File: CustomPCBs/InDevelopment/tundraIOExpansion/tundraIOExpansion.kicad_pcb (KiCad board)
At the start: 2 copper layers, 53 parts, among them J2 Conn_ARM_SWD_TagConnect_TC203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, J3 Conn_ARM_SWD_TagConnect_TC203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, U1 RP2040, U2 MX25L3233FM2, U4 MX25L3233FM2, U5 RP2040, Y1 Crystal, Y2 32.768kHz, Y3 Crystal

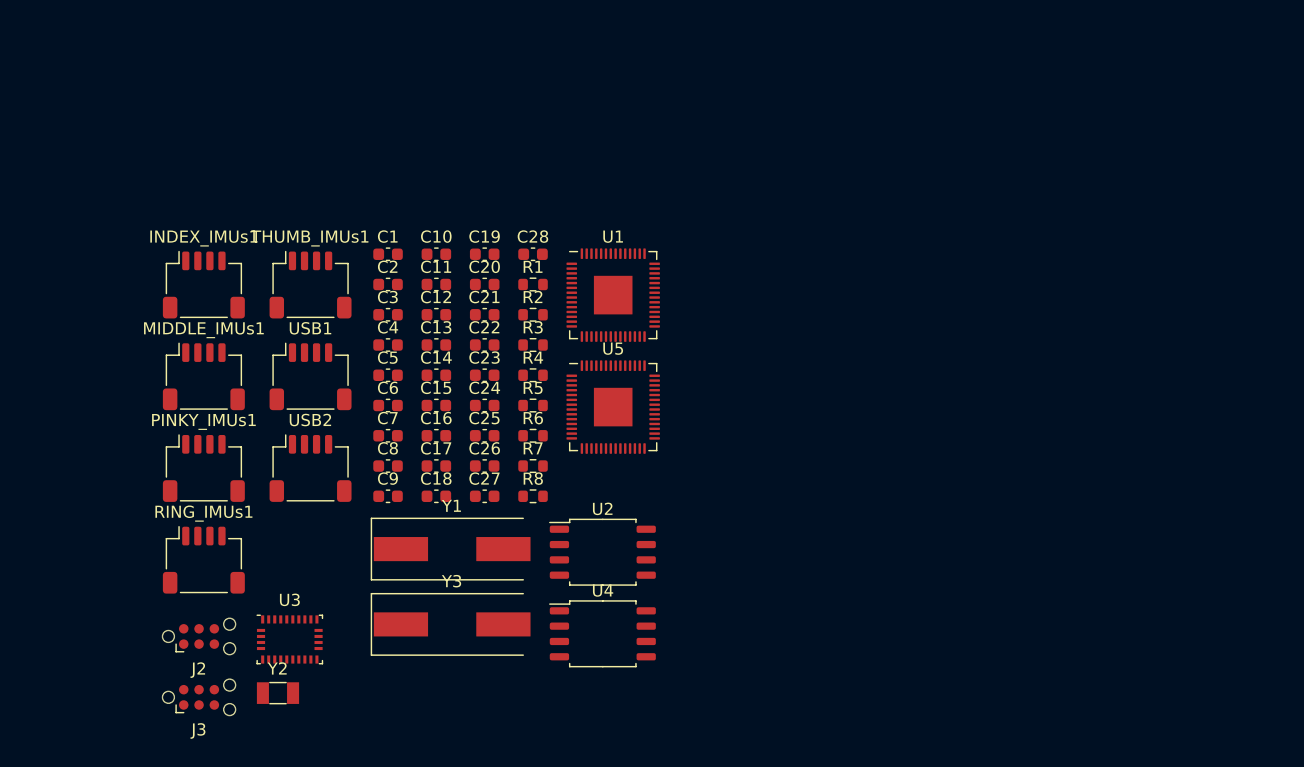
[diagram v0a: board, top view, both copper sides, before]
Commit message: Making outline for PCB
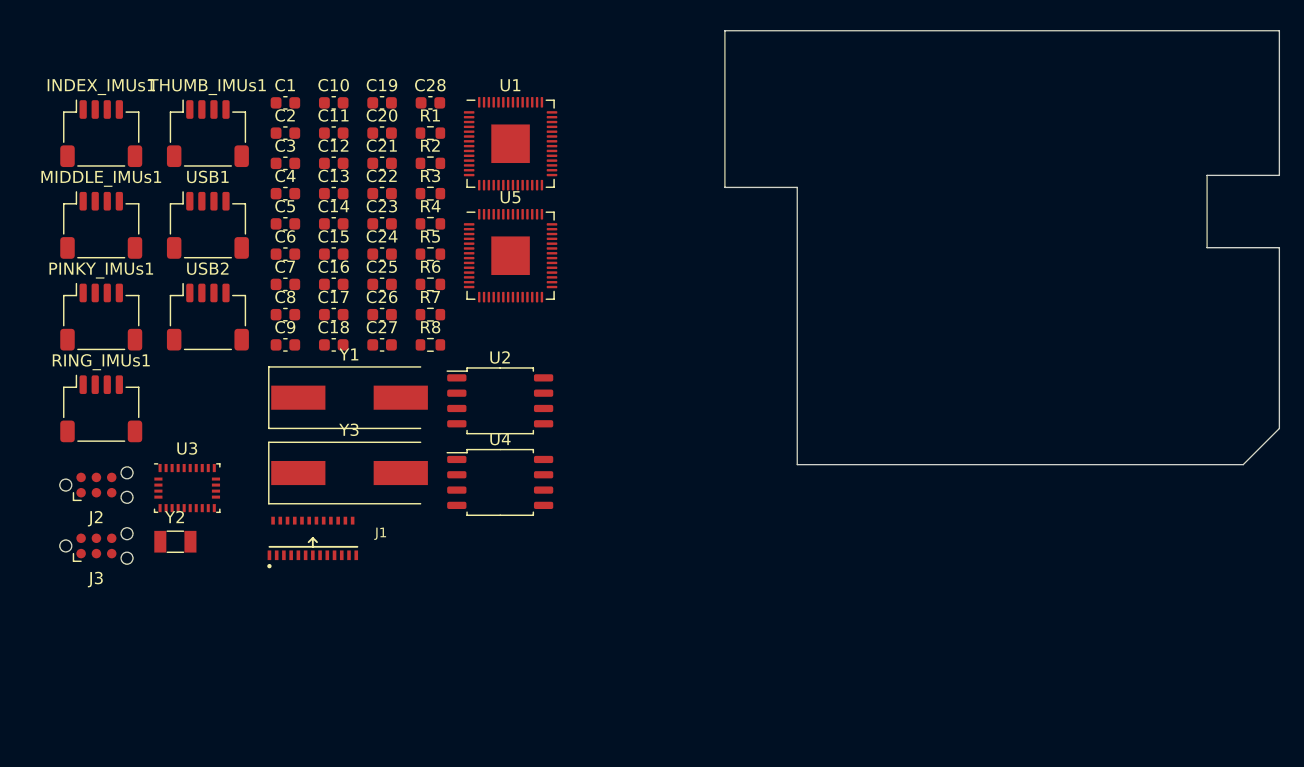
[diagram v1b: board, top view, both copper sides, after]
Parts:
- added J1: Conn_01x25, my_connectors:25PIN FRONT FLIP 0.6mm PITCH AYF332535A, F.Cu at (81.6, 99.2)
- moved THUMB_IMUs1 15.2 mm to (72.9, 65.6)
- moved U1 15.2 mm to (98.0, 66.5)
- moved U2 15.2 mm to (97.1, 87.8)
- moved U3 15.2 mm to (71.2, 95.0)
- moved U4 15.2 mm to (97.1, 94.6)
- moved U5 15.2 mm to (98.0, 75.8)
- moved USB1 15.2 mm to (72.9, 73.2)
- moved USB2 15.2 mm to (72.9, 80.8)
- moved Y1 15.2 mm to (84.6, 87.5)
- moved Y3 15.2 mm to (84.6, 93.8)
- moved J2 15.2 mm to (63.6, 94.8)
- moved J3 15.2 mm to (63.6, 99.8)
- moved C1 15.2 mm to (79.3, 63.1)
- moved C10 15.2 mm to (83.3, 63.1)
- moved C11 15.2 mm to (83.3, 65.6)
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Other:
- board outline added: 46 x 36 mm

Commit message: Connectors and ICs placed on rough locations
Also took care of board layout curves
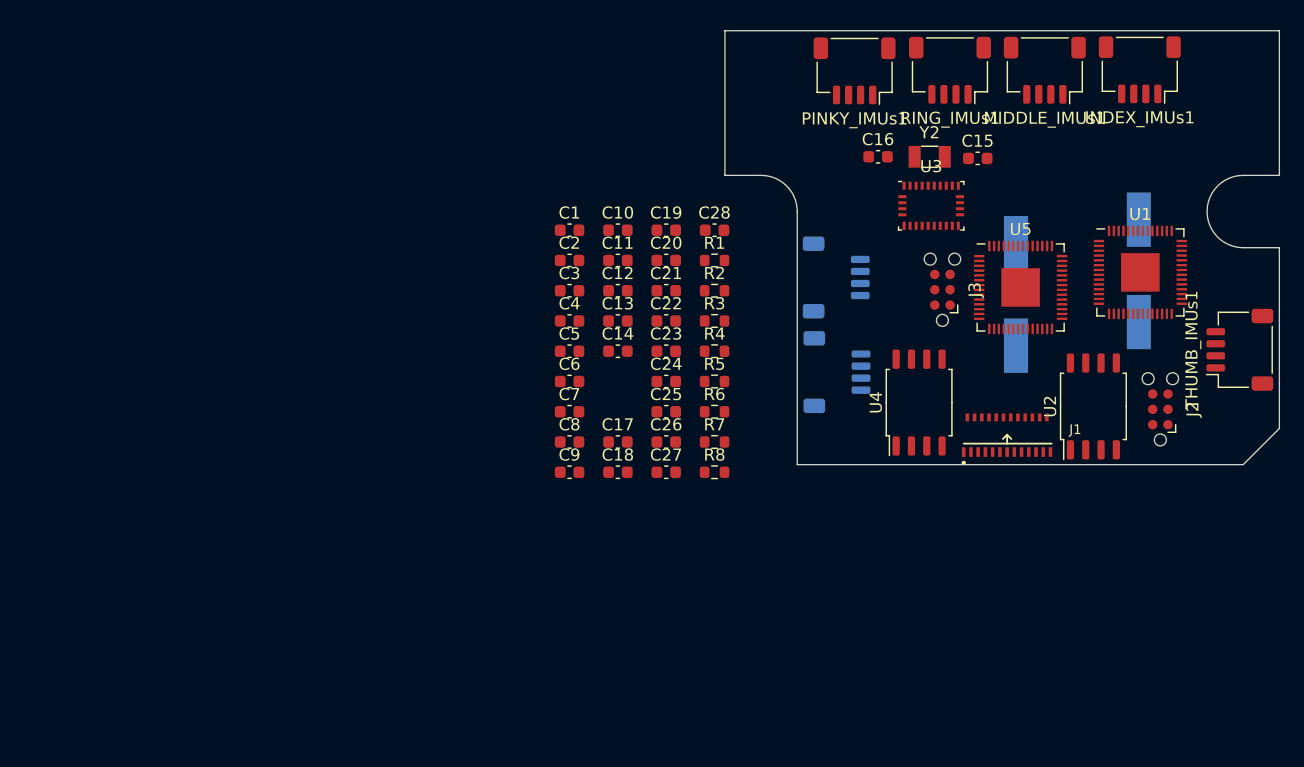
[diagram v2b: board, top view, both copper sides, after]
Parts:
- USB1, USB2, Y1, Y3: moved to B.Cu
- moved J2 88.5 mm to (151.9, 88.5), turned to 90 degrees
- moved THUMB_IMUs1 87.5 mm to (158.5, 83.6), turned to 90 degrees
- moved INDEX_IMUs1 86.3 mm to (150.2, 60.3), turned to 180 degrees
- moved MIDDLE_IMUs1 79.3 mm to (142.3, 60.4), turned to 180 degrees
- moved RING_IMUs1 75.8 mm to (134.4, 60.4), turned to 180 degrees
- moved J3 73.3 mm to (133.8, 78.6), turned to 90 degrees
- moved Y2 70.3 mm to (132.8, 67.5)
- moved Y1 66.3 mm to (150.1, 77.0), turned to -90 degrees
- moved U3 66.0 mm to (132.9, 71.6)
- moved PINKY_IMUs1 65.8 mm to (126.5, 60.4), turned to 180 degrees
- moved J1 58.2 mm to (139.2, 90.6)
- moved Y3 57.2 mm to (139.9, 79.0), turned to 90 degrees
- moved C15 54.0 mm to (136.8, 67.7)
- moved U1 53.3 mm to (150.2, 77.1)
- moved USB2 52.4 mm to (125.1, 85.4), turned to 90 degrees
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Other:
- outline, holes or cut-outs redrawn

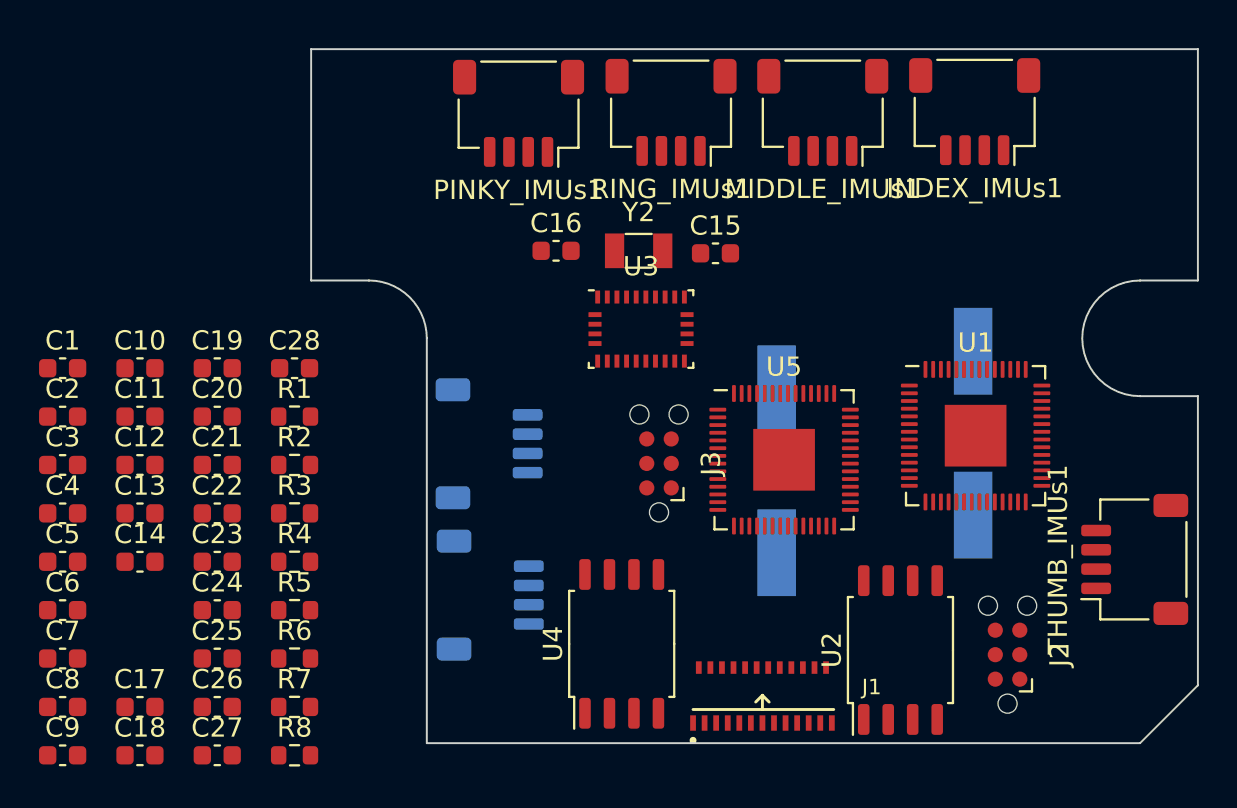
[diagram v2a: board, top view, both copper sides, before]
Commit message: Updating some footprints
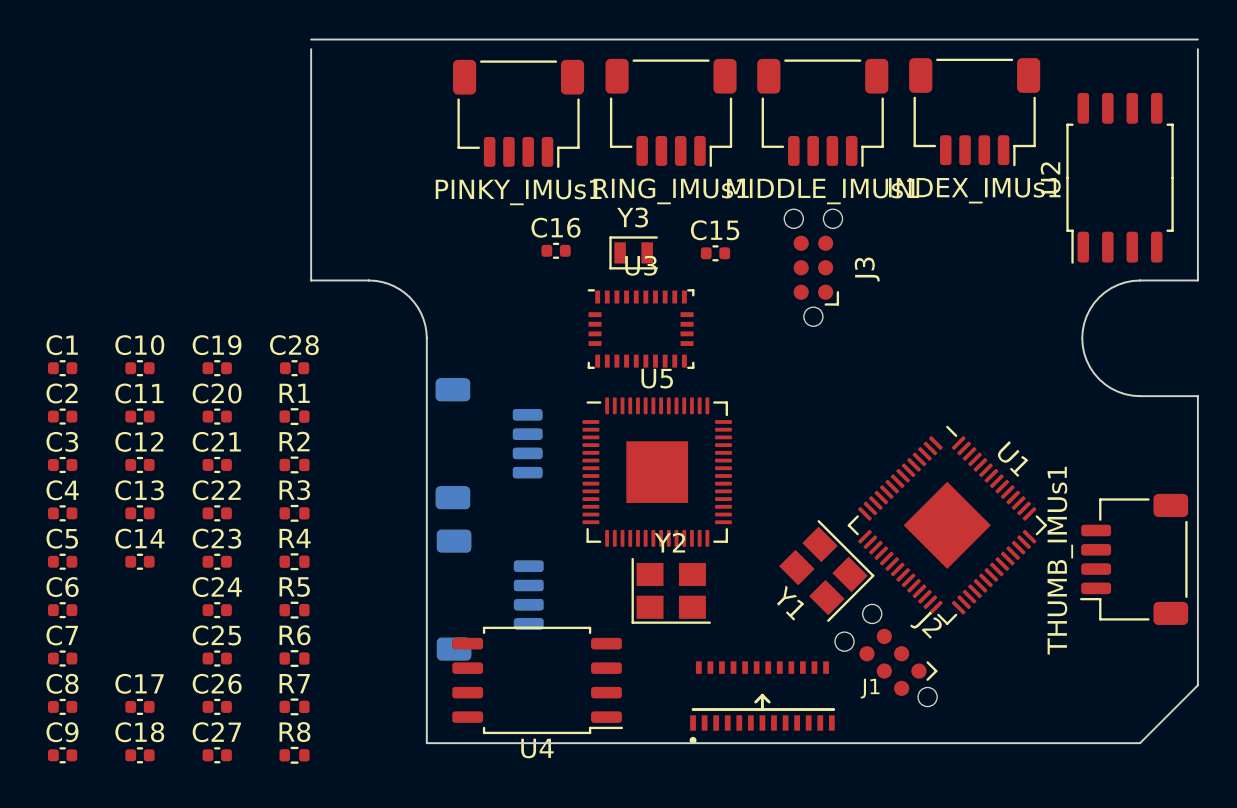
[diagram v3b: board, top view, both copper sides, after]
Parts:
- removed the Y3 at (139.9, 79.0)
- added Y2: 12.000MHz, Crystal:Crystal_SMD_3225-4Pin_3.2x2.5mm, F.Cu at (134.5, 85.2)
- C1, C10, C13, C14, C15, C16, C17, C18, C2, C20, C22, C23, C24, C25, C26, C27, C28, C3, C4, C5, C6, C7, C8, C9: footprint Capacitor_SMD:C_0603_1608Metric -> Capacitor_SMD:C_0402_1005Metric
- C11, C12, C19, C21: value 20p -> 27p; footprint Capacitor_SMD:C_0603_1608Metric -> Capacitor_SMD:C_0402_1005Metric
- R1, R2, R3, R4, R5, R6, R7, R8: footprint Resistor_SMD:R_0603_1608Metric -> Resistor_SMD:R_0402_1005Metric
- Y1: value Crystal -> 12.000MHz; footprint Crystal:Crystal_SMD_HC49-SD -> Crystal:Crystal_SMD_3225-4Pin_3.2x2.5mm; moved to F.Cu
- Y3: renamed from Y2; footprint Crystal:Crystal_SMD_3215-2Pin_3.2x1.5mm -> Crystal:Crystal_SMD_2012-2Pin_2.0x1.2mm
- moved U2 27.0 mm to (157.7, 63.8)
- moved J3 12.9 mm to (141.8, 68.4)
- moved Y1 10.6 mm to (142.4, 84.2), turned to 135 degrees
- moved U5 6.61 mm to (133.7, 79.0)
- moved J2 5.96 mm to (146.0, 88.9), turned to 135 degrees
- moved U1 4.88 mm to (148.8, 81.8), turned to -45 degrees
- moved U4 4.78 mm to (127.5, 89.8), turned to 180 degrees
- moved Y3 0.28 mm to (132.5, 67.7)
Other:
- board size 46 x 36 mm -> 46 x 36.5 mm
- copper layers 2 -> 4

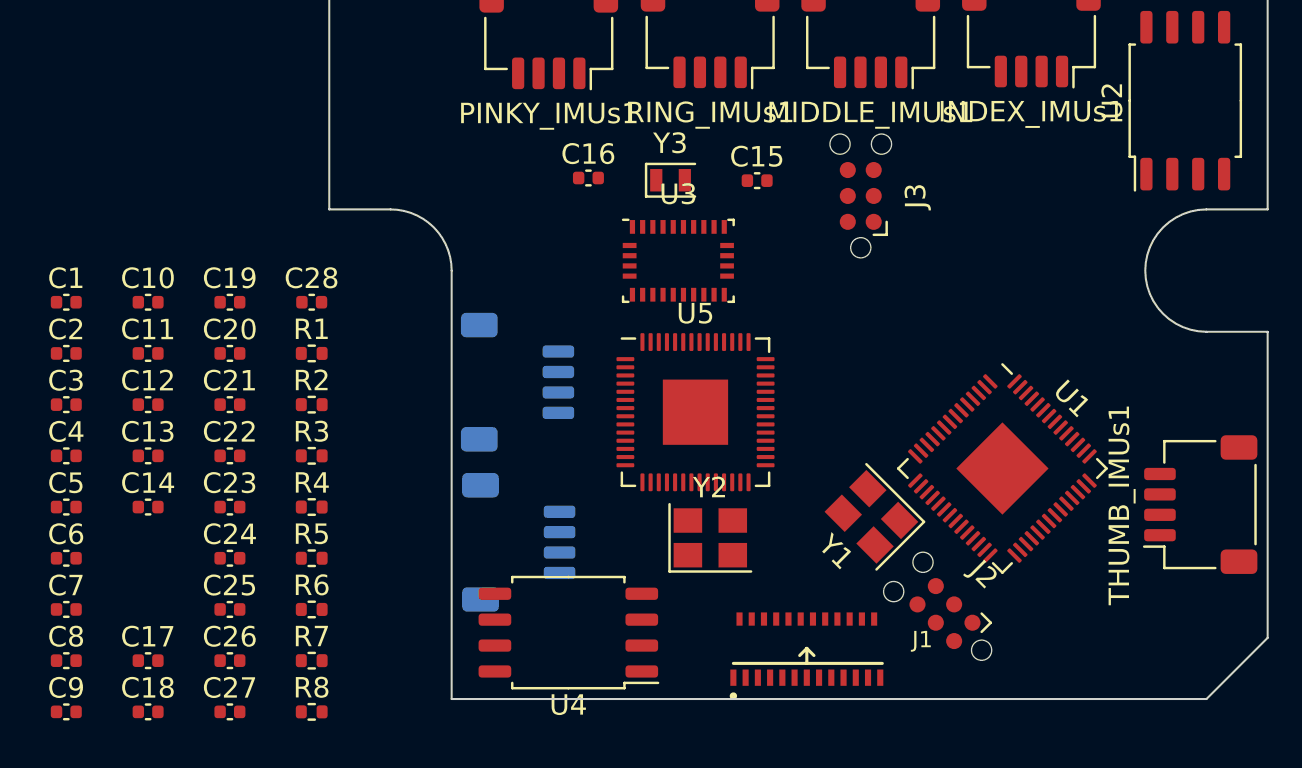
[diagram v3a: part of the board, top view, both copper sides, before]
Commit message: Most components placed on tundra interface pcb
Decoupling caps next and then maybe adding some more connectors where
possible for future functionality expansion
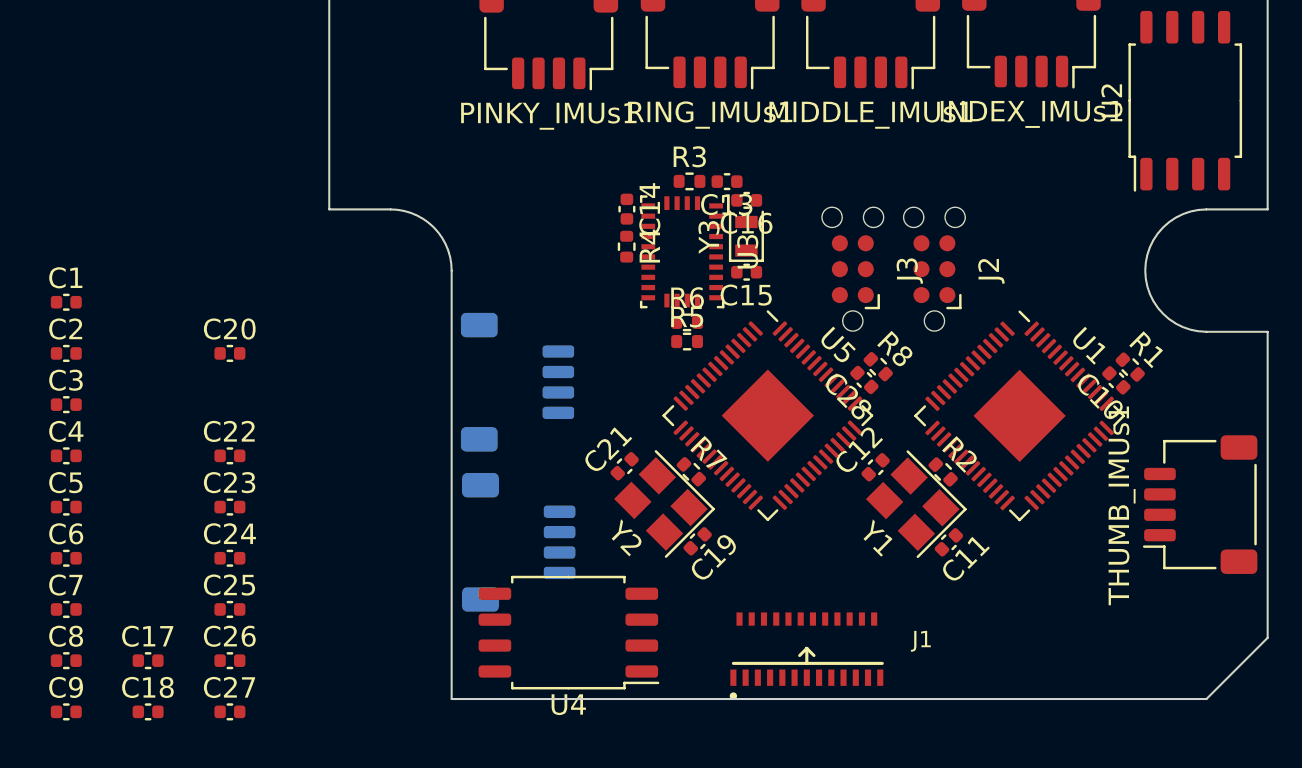
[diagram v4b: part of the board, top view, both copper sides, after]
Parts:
- moved C10 47.6 mm to (154.4, 77.5), turned to 135 degrees
- moved C11 40.3 mm to (146.2, 85.4), turned to -135 degrees
- moved R1 40.1 mm to (155.0, 76.8), turned to -45 degrees
- moved C12 35.8 mm to (142.6, 81.7), turned to 45 degrees
- moved R8 32.5 mm to (142.7, 76.8), turned to -45 degrees
- moved C13 31.4 mm to (135.3, 67.7), turned to 180 degrees
- moved R2 31.1 mm to (145.9, 82.0), turned to -45 degrees
- moved C14 27.6 mm to (130.4, 69.1), turned to -90 degrees
- moved C28 27.4 mm to (142.0, 77.5), turned to 135 degrees
- moved C19 25.8 mm to (133.8, 85.4), turned to -135 degrees
- moved R6 23.2 mm to (133.3, 74.6)
- moved R3 22.9 mm to (133.4, 67.7)
- moved R5 21.2 mm to (133.3, 75.6)
- moved R7 20.8 mm to (133.5, 82.0), turned to -45 degrees
- moved R4 20.0 mm to (130.4, 70.9), turned to -90 degrees
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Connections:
- Y1 pad 2: Net-(C12-Pad1) -> GND
- Y1 pad 3: (no net) -> Net-(C12-Pad1)
- Y1 pad 4: (no net) -> GND
- Y2 pad 2: Net-(C21-Pad1) -> GND
- Y2 pad 3: (no net) -> Net-(C21-Pad1)
- Y2 pad 4: (no net) -> GND
